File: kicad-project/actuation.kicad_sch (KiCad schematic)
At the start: 14 parts

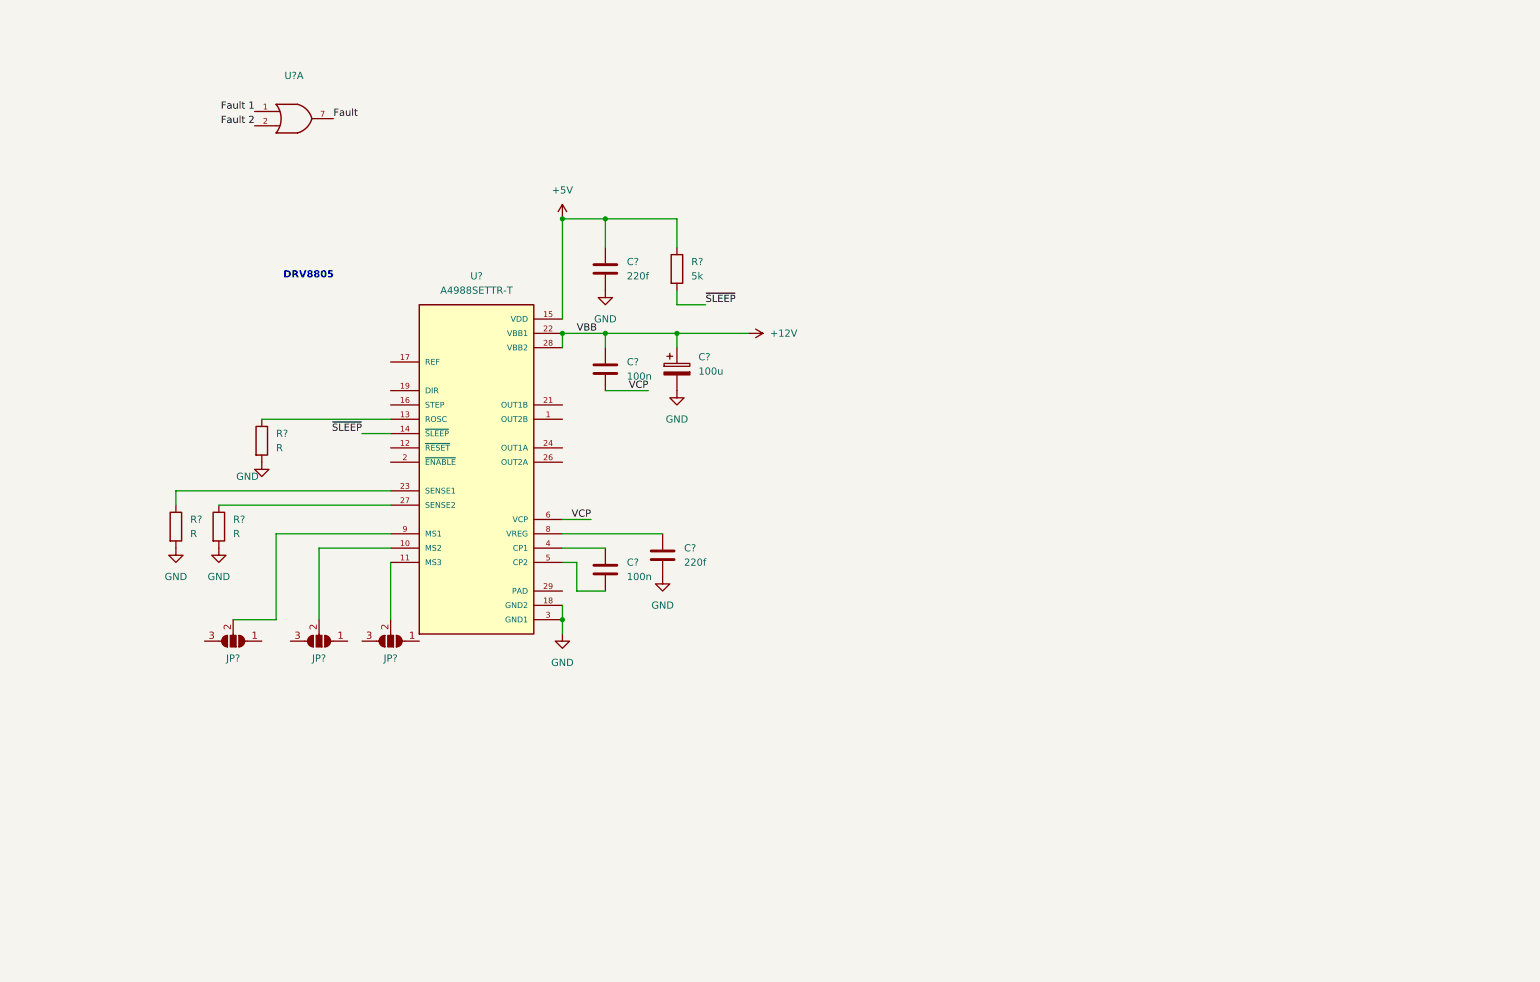
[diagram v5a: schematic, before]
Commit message: hw: add stepper motor drivers
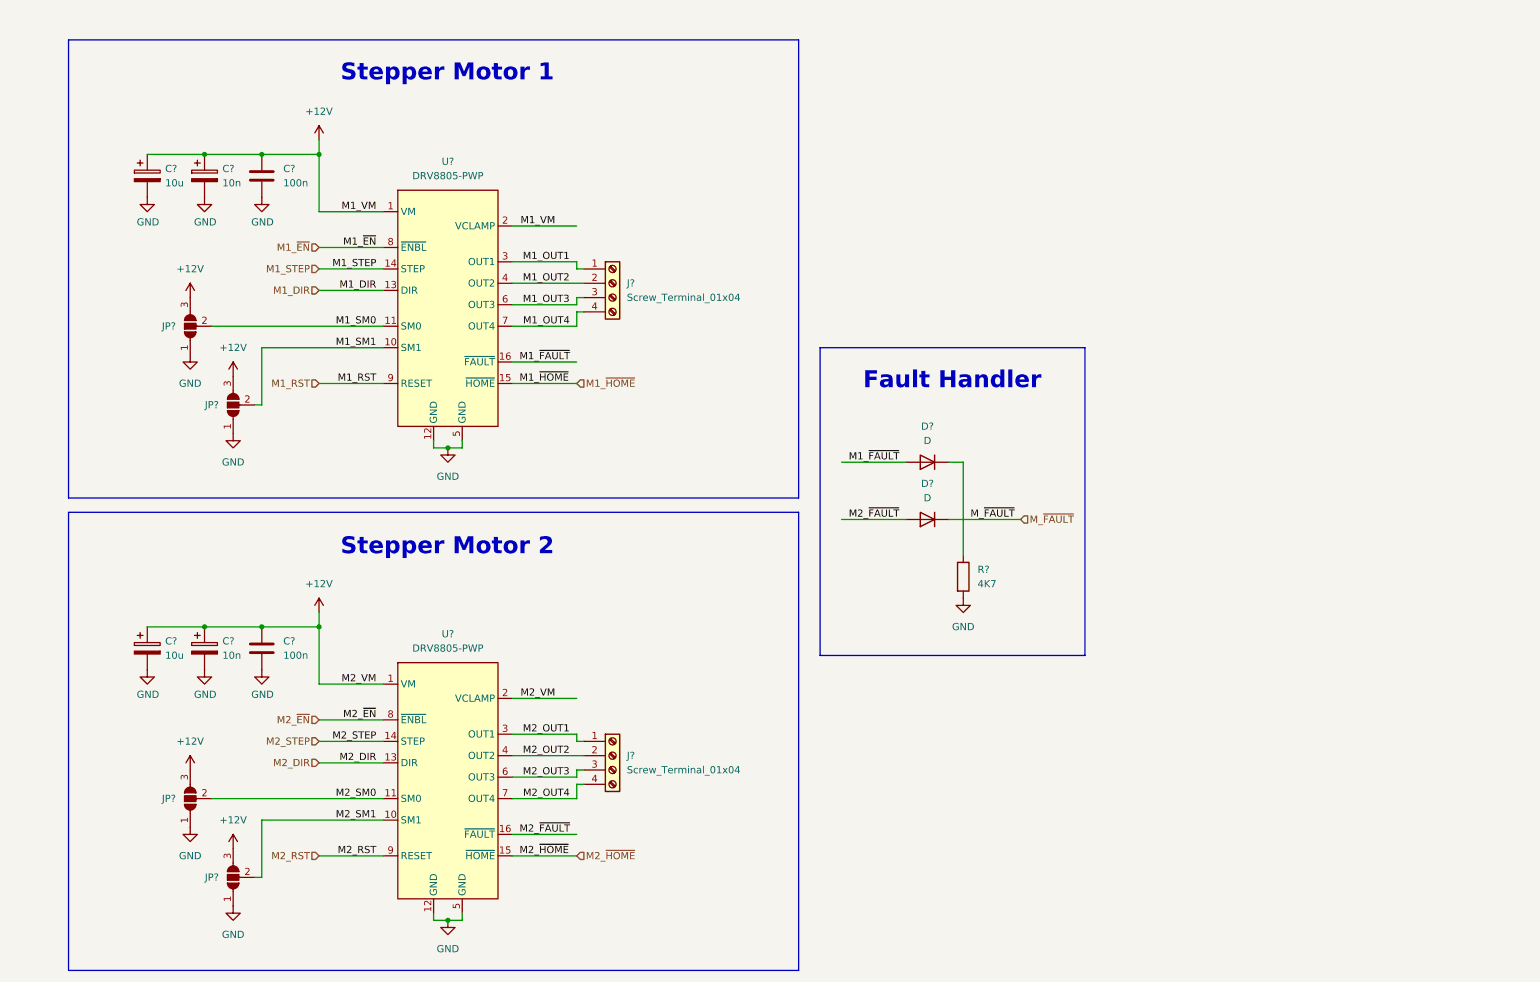
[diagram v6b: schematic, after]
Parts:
- removed C? (x2): 220f, symbol Device:C
- removed C? (x2): 100n, symbol Device:C
- removed C?: 100u, symbol Device:C_Polarized
- removed JP?: SolderJumper_3_Open, symbol Jumper:SolderJumper_3_Open
- removed R? (x3): R, symbol Device:R
- removed R?: 5k, symbol Device:R
- removed U?: A4988SETTR-T, QFN50P500X500X90-29N, symbol A4988:A4988SETTR-T
- removed U?: (no value), symbol 74xGxx:74AUC2G32
- added C? (x2): 10n, symbol Device:C_Polarized
- added C? (x2): 100n, symbol Device:C
- added C? (x2): 10u, symbol Device:C_Polarized
- added D? (x2): D, symbol Device:D
- added J? (x2): Screw_Terminal_01x04, symbol Connector:Screw_Terminal_01x04
- added JP? (x2): SolderJumper_3_Open, symbol Jumper:SolderJumper_3_Open
- added R?: 4K7, symbol Device:R
- added U? (x2): DRV8805-PWP, symbol PPSE_2021:DRV8805-PWP
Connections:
- net +12V: now also JP?.3 (B), JP?.3 (B), C?.1, C?.1, C?.1, C?.1, C?.1, C?.1, JP?.3 (B), JP?.3 (B), U?.1 (VM), U?.1 (VM), U?.2 (VCLAMP), U?.2 (VCLAMP)
- net GND: now also JP?.1 (A), JP?.1 (A), C?.2, C?.2, C?.2, C?.2, C?.2, C?.2, JP?.1 (A), JP?.1 (A), R?.2, U?.12 (GND), U?.12 (GND), U?.5 (GND), U?.5 (GND)
- net M1_SM0: now reaches JP?.2 (C)
- net M1_SM0: now also U?.11 (SM0)
- net M1_SM1: now reaches JP?.2 (C)
- net M1_SM1: now also U?.10 (SM1)
- new net: D?.1 (K), R?.1
- new net M1_DIR: U?.13 (DIR)
- new net M1_OUT1: J?.1 (Pin_1), U?.3 (OUT1)
- new net M1_OUT2: J?.2 (Pin_2), U?.4 (OUT2)
- new net M1_OUT3: J?.3 (Pin_3), U?.6 (OUT3)
- new net M1_OUT4: J?.4 (Pin_4), U?.7 (OUT4)
- new net M1_RST: U?.9 (RESET)
- new net M1_STEP: U?.14 (STEP)
- new net M1_~{EN}: U?.8 (~{ENBL})
- new net M1_~{FAULT}: D?.2 (A), U?.16 (~{FAULT})
- new net M1_~{HOME}: U?.15 (~{HOME})
- new net M2_DIR: U?.13 (DIR)
- new net M2_OUT1: J?.1 (Pin_1), U?.3 (OUT1)
- new net M2_OUT2: J?.2 (Pin_2), U?.4 (OUT2)
- new net M2_OUT3: J?.3 (Pin_3), U?.6 (OUT3)
- new net M2_OUT4: J?.4 (Pin_4), U?.7 (OUT4)
- new net M2_RST: U?.9 (RESET)
- new net M2_SM0: JP?.2 (C), U?.11 (SM0)
- new net M2_SM1: JP?.2 (C), U?.10 (SM1)
- new net M2_STEP: U?.14 (STEP)
- new net M2_~{EN}: U?.8 (~{ENBL})
- new net M2_~{FAULT}: D?.2 (A), U?.16 (~{FAULT})
- new net M2_~{HOME}: U?.15 (~{HOME})
- new net M_~{FAULT}: D?.1 (K)
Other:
- note added: "Fault Handler"
- note added: "Stepper Motor 1"
- note added: "Stepper Motor 2"
- note removed: "DRV8805"
- moved on the sheet: JP?

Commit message: hw: move inputs from control to sensing and outputs from control to actuation
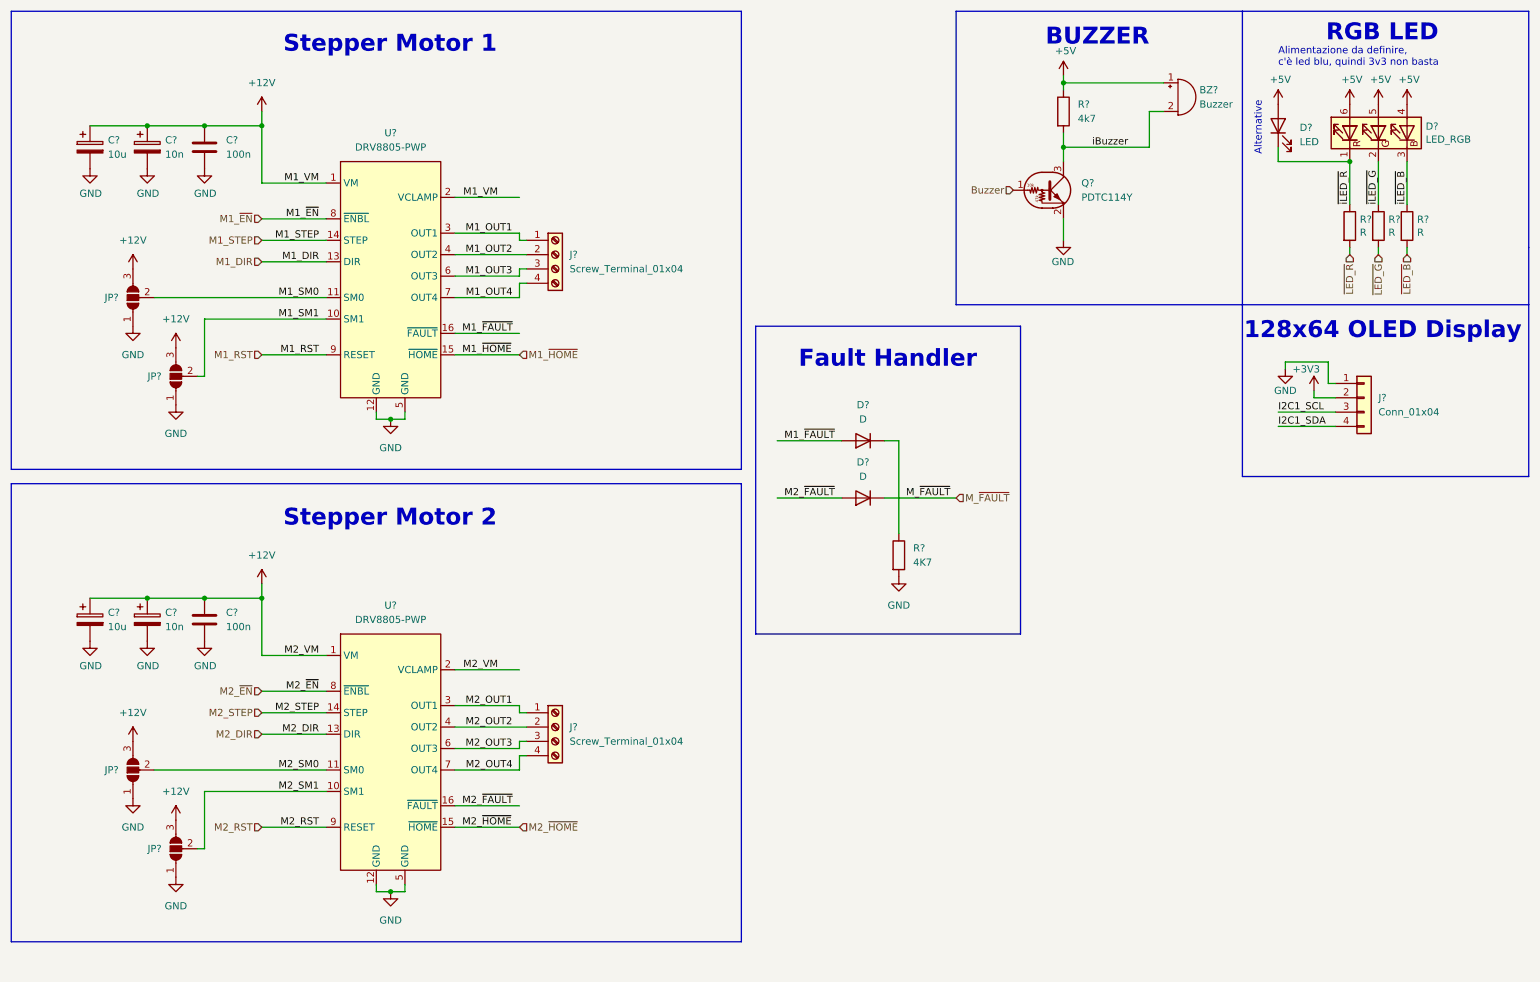
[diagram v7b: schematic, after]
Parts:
- added BZ?: Buzzer, symbol Device:Buzzer
- added D?: LED, symbol Device:LED
- added D?: LED_RGB, symbol Device:LED_RGB
- added J?: Conn_01x04, symbol Connector_Generic:Conn_01x04
- added Q?: PDTC114Y, symbol Transistor_BJT:DTC114Y
- added R?: 4k7, symbol Device:R
- added R? (x3): R, symbol Device:R
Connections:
- net GND: now also J?.1 (Pin_1), Q?.2 (E)
- new net +3V3: J?.2 (Pin_2)
- new net +5V: BZ?.1 (-), D?.2 (A), D?.4 (BA), D?.5 (GA), D?.6 (RA), R?.1
- new net Buzzer: Q?.1 (B)
- new net I2C1_SCL: J?.3 (Pin_3)
- new net I2C1_SDA: J?.4 (Pin_4)
- new net iBuzzer: BZ?.2 (+), Q?.3 (C), R?.2
- new net ~{LED_B}: R?.2
- new net ~{LED_G}: R?.2
- new net ~{LED_R}: R?.2
- new net ~{iLED_B}: D?.3 (BK), R?.1
- new net ~{iLED_G}: D?.2 (GK), R?.1
- new net ~{iLED_R}: D?.1 (K), D?.1 (RK), R?.1
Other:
- note added: "128x64 OLED Display"
- note added: "Alimentazione da definire, c'è led blu, quindi 3v3 non basta"
- note added: "Alternative"
- note added: "BUZZER"
- note added: "RGB LED"
- moved on the sheet: C?, D?, J?, JP?, R?, U?

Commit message: fw: discrete dirver for stepper
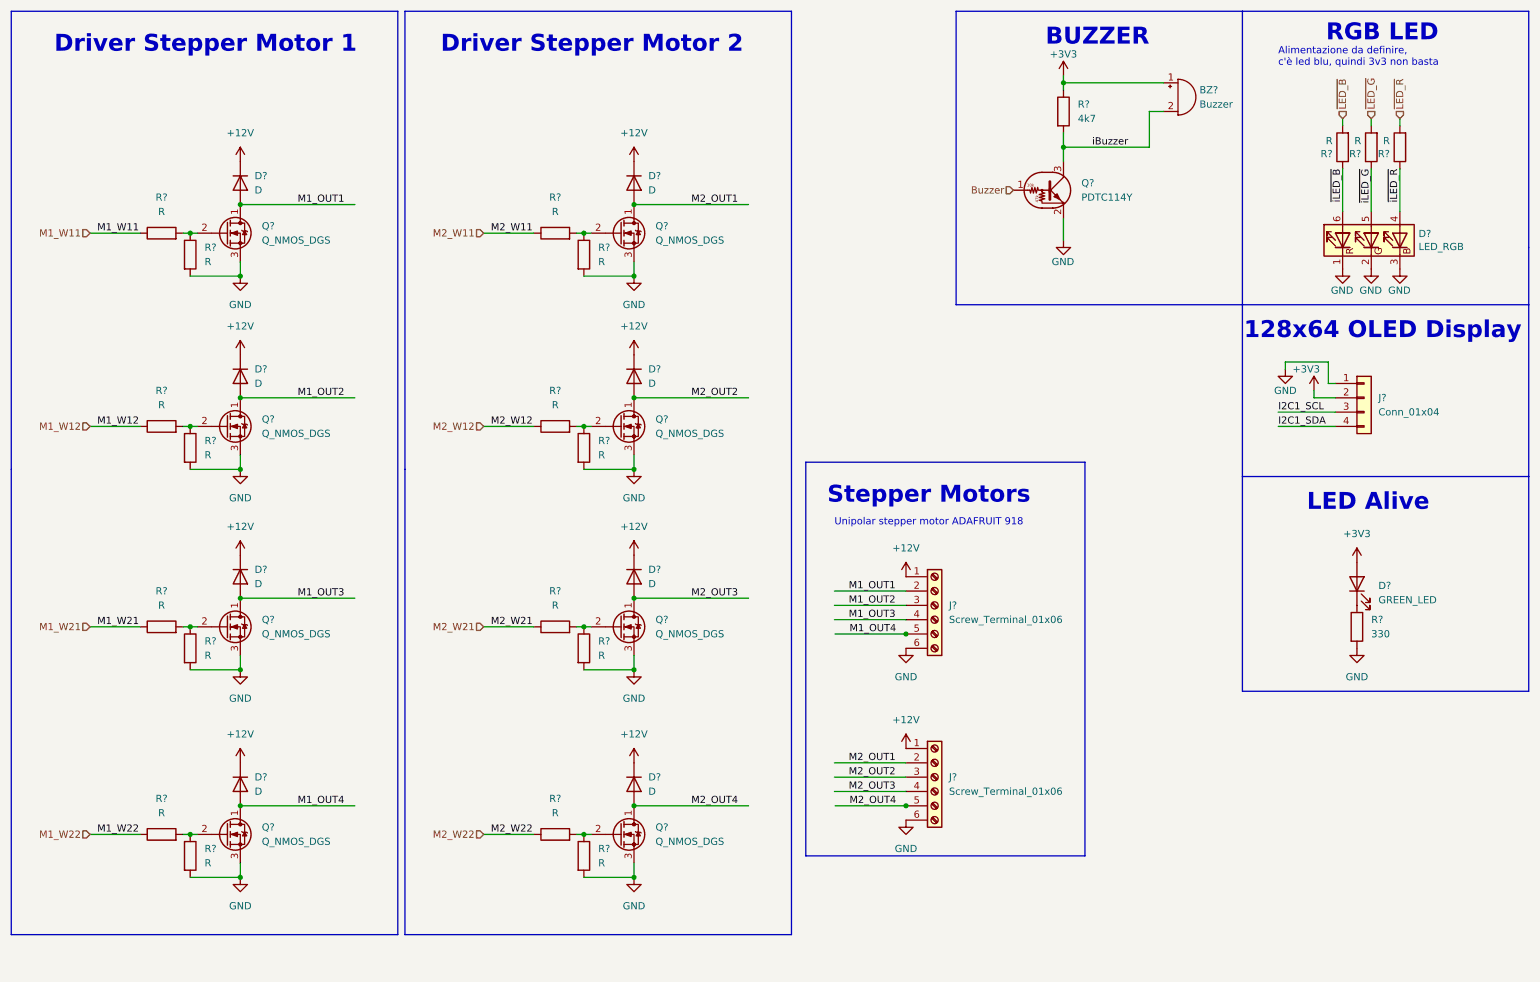
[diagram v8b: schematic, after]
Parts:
- removed C? (x2): 10n, symbol Device:C_Polarized
- removed C? (x2): 100n, symbol Device:C
- removed C? (x2): 10u, symbol Device:C_Polarized
- removed D?: LED, symbol Device:LED
- removed D? (x2): D, symbol Device:D
- removed J? (x2): Screw_Terminal_01x04, symbol Connector:Screw_Terminal_01x04
- removed JP? (x4): SolderJumper_3_Open, symbol Jumper:SolderJumper_3_Open
- removed R?: 4K7, symbol Device:R
- removed U? (x2): DRV8805-PWP, symbol PPSE_2021:DRV8805-PWP
- added D? (x8): D, symbol Device:D
- added D?: GREEN_LED, symbol Device:LED
- added J? (x2): Screw_Terminal_01x06, symbol Connector:Screw_Terminal_01x06
- added Q? (x8): Q_NMOS_DGS, symbol Device:Q_NMOS_DGS
- added R? (x16): R, symbol Device:R
- added R?: 330, symbol Device:R
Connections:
- net +12V: now also D?.1 (K), D?.1 (K), D?.1 (K), D?.1 (K), D?.1 (K), D?.1 (K), D?.1 (K), D?.1 (K), J?.1 (Pin_1), J?.1 (Pin_1)
- net +3V3: now also BZ?.1 (-), R?.1, D?.2 (A)
- net GND: now also D?.1 (RK), D?.2 (GK), D?.3 (BK), J?.6 (Pin_6), J?.6 (Pin_6), Q?.3 (S), Q?.3 (S), Q?.3 (S), Q?.3 (S), Q?.3 (S), Q?.3 (S), Q?.3 (S), Q?.3 (S), R?.2, R?.2, R?.2, R?.2, R?.2, R?.2, R?.2, R?.2, R?.2
- net M1_OUT1: now also D?.2 (A), J?.2 (Pin_2), Q?.1 (D)
- net M1_OUT2: now also D?.2 (A), J?.3 (Pin_3), Q?.1 (D)
- net M1_OUT3: now also D?.2 (A), J?.4 (Pin_4), Q?.1 (D)
- net M1_OUT4: now also D?.2 (A), J?.5 (Pin_5), Q?.1 (D)
- net M2_OUT1: now also D?.2 (A), J?.2 (Pin_2), Q?.1 (D)
- net M2_OUT2: now also D?.2 (A), J?.3 (Pin_3), Q?.1 (D)
- net M2_OUT3: now also D?.2 (A), J?.4 (Pin_4), Q?.1 (D)
- net M2_OUT4: now also D?.2 (A), J?.5 (Pin_5), Q?.1 (D)
- net ~{iLED_B}: now also D?.6 (RA); no longer D?.3 (BK)
- net ~{iLED_G}: now also D?.5 (GA); no longer D?.2 (GK)
- net ~{iLED_R}: now also D?.4 (BA); no longer D?.1 (RK)
- removed net +5V: BZ?.1 (-), D?.4 (BA), D?.5 (GA), D?.6 (RA), R?.1
- new net: Q?.2 (G), R?.1, R?.2 (x8)
- new net: D?.1 (K), R?.1
- new net M1_W11: R?.1
- new net M1_W12: R?.1
- new net M1_W21: R?.1
- new net M1_W22: R?.1
- new net M2_W11: R?.1
- new net M2_W12: R?.1
- new net M2_W21: R?.1
- new net M2_W22: R?.1
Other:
- note added: "Driver Stepper Motor 1"
- note added: "Driver Stepper Motor 2"
- note added: "LED Alive"
- note added: "Stepper Motors"
- note added: "Unipolar stepper motor ADAFRUIT 918"
- note removed: "Alternative"
- note removed: "Fault Handler"
- note removed: "Stepper Motor 1"
- note removed: "Stepper Motor 2"
- moved on the sheet: D?, R?
